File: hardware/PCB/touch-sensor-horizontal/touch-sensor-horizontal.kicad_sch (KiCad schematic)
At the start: 2 parts, among them J1 touch-sensor

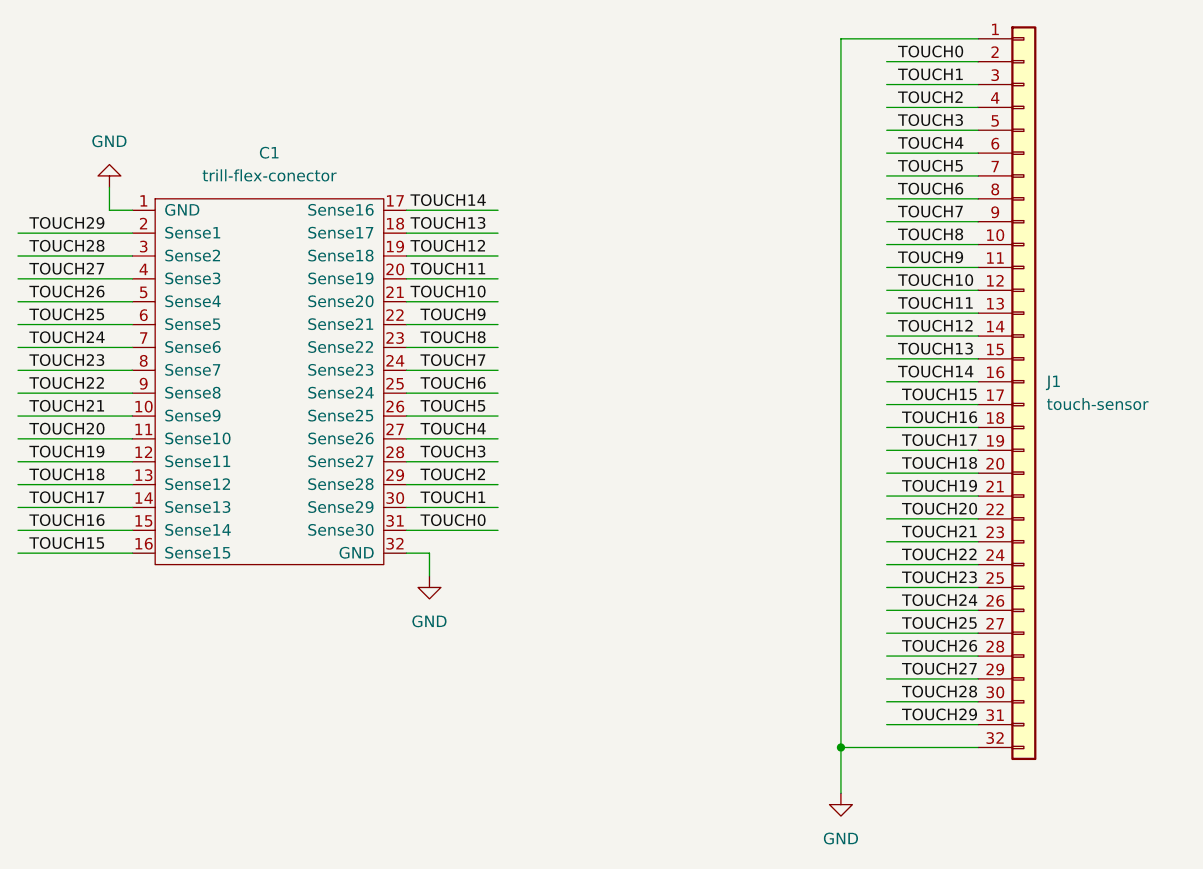
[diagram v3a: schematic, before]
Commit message: extended length of slider back to 30cm
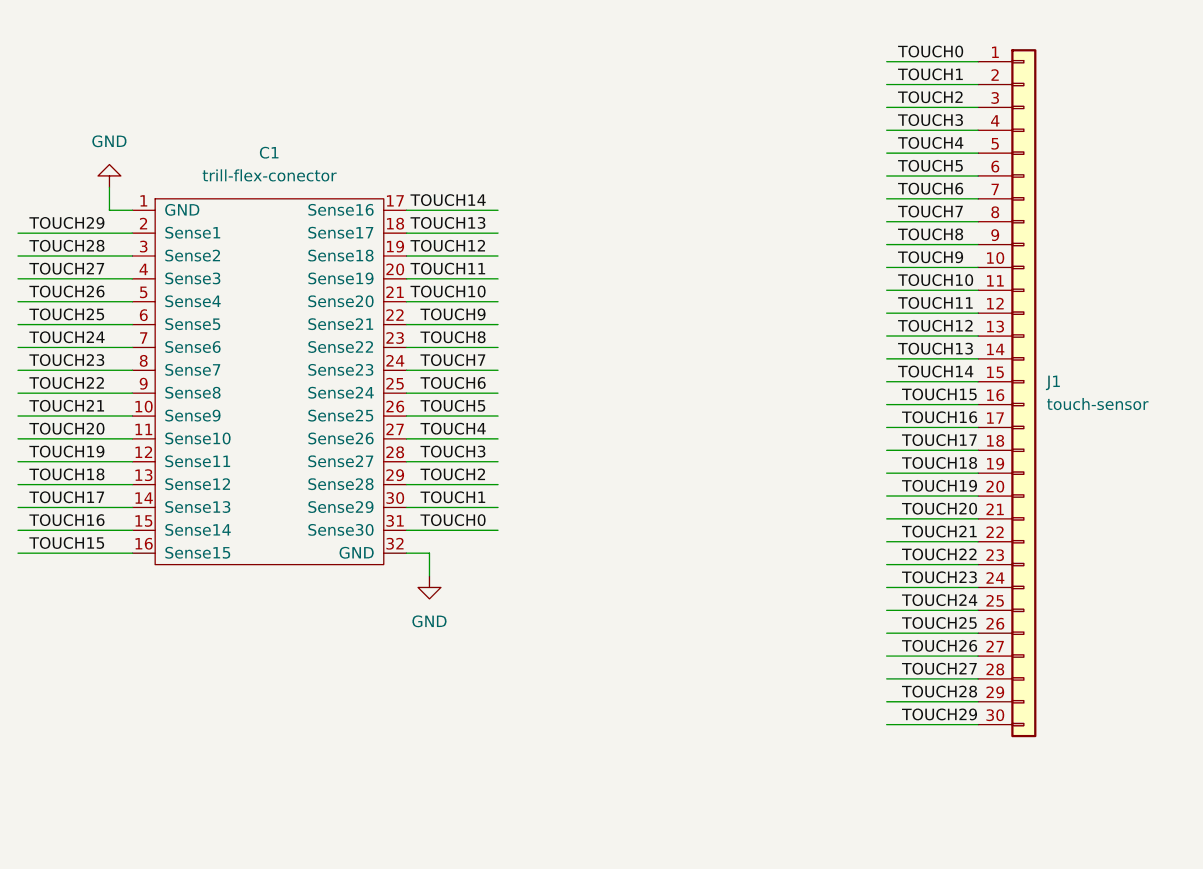
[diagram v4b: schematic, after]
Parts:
- J1: symbol Connector_Generic:Conn_01x32 -> Connector_Generic:Conn_01x30
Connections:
- net GND: no longer J1.1 (Pin_1), J1.32 (Pin_32)
- net TOUCH0: now also J1.1 (Pin_1); no longer J1.2 (Pin_2)
- net TOUCH1: now also J1.2 (Pin_2); no longer J1.3 (Pin_3)
- net TOUCH10: now also J1.11 (Pin_11); no longer J1.12 (Pin_12)
- net TOUCH11: now also J1.12 (Pin_12); no longer J1.13 (Pin_13)
- net TOUCH12: now also J1.13 (Pin_13); no longer J1.14 (Pin_14)
- net TOUCH13: now also J1.14 (Pin_14); no longer J1.15 (Pin_15)
- net TOUCH14: now also J1.15 (Pin_15); no longer J1.16 (Pin_16)
- net TOUCH15: now also J1.16 (Pin_16); no longer J1.17 (Pin_17)
- net TOUCH16: now also J1.17 (Pin_17); no longer J1.18 (Pin_18)
- net TOUCH17: now also J1.18 (Pin_18); no longer J1.19 (Pin_19)
- net TOUCH18: now also J1.19 (Pin_19); no longer J1.20 (Pin_20)
- net TOUCH19: now also J1.20 (Pin_20); no longer J1.21 (Pin_21)
- net TOUCH2: now also J1.3 (Pin_3); no longer J1.4 (Pin_4)
- net TOUCH20: now also J1.21 (Pin_21); no longer J1.22 (Pin_22)
- net TOUCH21: now also J1.22 (Pin_22); no longer J1.23 (Pin_23)
- net TOUCH22: now also J1.23 (Pin_23); no longer J1.24 (Pin_24)
- net TOUCH23: now also J1.24 (Pin_24); no longer J1.25 (Pin_25)
- net TOUCH24: now also J1.25 (Pin_25); no longer J1.26 (Pin_26)
- net TOUCH25: now also J1.26 (Pin_26); no longer J1.27 (Pin_27)
- net TOUCH26: now also J1.27 (Pin_27); no longer J1.28 (Pin_28)
- net TOUCH27: now also J1.28 (Pin_28); no longer J1.29 (Pin_29)
- net TOUCH28: now also J1.29 (Pin_29); no longer J1.30 (Pin_30)
- net TOUCH29: now also J1.30 (Pin_30); no longer J1.31 (Pin_31)
- net TOUCH3: now also J1.4 (Pin_4); no longer J1.5 (Pin_5)
- net TOUCH4: now also J1.5 (Pin_5); no longer J1.6 (Pin_6)
- net TOUCH5: now also J1.6 (Pin_6); no longer J1.7 (Pin_7)
- net TOUCH6: now also J1.7 (Pin_7); no longer J1.8 (Pin_8)
- net TOUCH7: now also J1.8 (Pin_8); no longer J1.9 (Pin_9)
- net TOUCH8: now also J1.9 (Pin_9); no longer J1.10 (Pin_10)
- net TOUCH9: now also J1.10 (Pin_10); no longer J1.11 (Pin_11)
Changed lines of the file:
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@@
 (kicad_sch (version 20230121) (generator eeschema)
   (paper "A4")
-  (junction (at 143.51 121.92) (diameter 0) (color 0 0 0 0)
-  )
   (wire (pts (xy 148.59 91.44) (xy 158.75 91.44))
     (stroke (width 0) (type default))
@@
     (stroke (width 0) (type default))
   )
-  (wire (pts (xy 143.51 121.92) (xy 158.75 121.92))
-    (stroke (width 0) (type default))
-  )
-  (wire (pts (xy 158.75 43.18) (xy 143.51 43.18))
-    (stroke (width 0) (type default))
-  )
   (wire (pts (xy 105.41 82.55) (xy 95.25 82.55))
     (stroke (width 0) (type default))
@@
     (stroke (width 0) (type default))
   )
-  (wire (pts (xy 143.51 43.18) (xy 143.51 121.92))
-    (stroke (width 0) (type default))
-  )
   (wire (pts (xy 105.41 72.39) (xy 95.25 72.39))
     (stroke (width 0) (type default))
@@
     (stroke (width 0) (type default))
   )
-  (wire (pts (xy 143.51 121.92) (xy 143.51 127))
-    (stroke (width 0) (type default))
-  )
   (wire (pts (xy 148.59 101.6) (xy 158.75 101.6))
     (stroke (width 0) (type default))
@@
   (label "TOUCH17" (at 53.34 95.25 0) (fields_autoplaced)
     (effects (font (size 1.27 1.27)) (justify left bottom))
-  )
-  (symbol (lib_id "power:GND") (at 143.51 127 0) (unit 1)
-    (in_bom yes) (on_board yes) (dnp no) (fields_autoplaced)
-    (property "Reference" "#PWR03" (at 143.51 133.35 0)
-      (effects (font (size 1.27 1.27)) hide)
-    )
-    (property "Value" "GND" (at 143.51 132.08 0)
-      (effects (font (size 1.27 1.27)))
-    )
-    (property "Footprint" "" (at 143.51 127 0)
-      (effects (font (size 1.27 1.27)) hide)
-    )
-    (property "Datasheet" "" (at 143.51 127 0)
-      (effects (font (size 1.27 1.27)) hide)
-    )
-    (pin "1")
-    (instances
-      (project "touch-sensor-horizontal"
-        (path "/beaa8ee0-3ec8-40a6-99fa-0f4d6fddebd1"
-          (reference "#PWR03") (unit 1)
-        )
-      )
-    )
   )
   (symbol (lib_id "trill-flex:trill-flex-conector") (at 80.01 59.69 0) (unit 1)
@@
     )
   )
-  (symbol (lib_id "Connector_Generic:Conn_01x32") (at 163.83 81.28 0) (unit 1)
+  (symbol (lib_id "Connector_Generic:Conn_01x30") (at 163.83 81.28 0) (unit 1)
     (in_bom yes) (on_board yes) (dnp no) (fields_autoplaced)
     (property "Reference" "J1" (at 166.37 81.28 0)
@@
     (pin "8")
     (pin "9")
-    (pin "31")
-    (pin "32")
     (instances
       (project "touch-sensor-horizontal"
